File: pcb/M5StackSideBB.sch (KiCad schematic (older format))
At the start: 4 parts, among them J1 Conn_01x11, J2 Conn_01x11, J3 Conn_02x15_Odd_Even, J4 Conn_02x15_Odd_Even

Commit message: Assign footprint of pin socket without silk
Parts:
- J1, J2: footprint Connector_PinSocket_2.54mm:PinSocket_1x11_P2.54mm_Vertical -> footprints:PinSocket_1x11_P2.54mm_Vertical_without_silk
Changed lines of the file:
@@
 F 0 "J1" H 5150 3600 50  0000 L CNN
 F 1 "Conn_01x11" H 5000 3500 50  0000 L CNN
-F 2 "Connector_PinSocket_2.54mm:PinSocket_1x11_P2.54mm_Vertical" H 5150 2850 50  0001 C CNN
+F 2 "footprints:PinSocket_1x11_P2.54mm_Vertical_without_silk" H 5150 2850 50  0001 C CNN
 F 3 "~" H 5150 2850 50  0001 C CNN
 	1    5150 2850
@@
 F 0 "J2" H 6200 3600 50  0000 L CNN
 F 1 "Conn_01x11" H 6050 3500 50  0000 L CNN
-F 2 "Connector_PinSocket_2.54mm:PinSocket_1x11_P2.54mm_Vertical" H 6200 2850 50  0001 C CNN
+F 2 "footprints:PinSocket_1x11_P2.54mm_Vertical_without_silk" H 6200 2850 50  0001 C CNN
 F 3 "~" H 6200 2850 50  0001 C CNN
 	1    6200 2850
@@
 G34
 $Comp
-L power:+5V #PWR?
+L power:+5V #PWR0101
 U 1 1 5B50EF03
 P 7650 3600
-F 0 "#PWR?" H 7650 3450 50  0001 C CNN
+F 0 "#PWR0101" H 7650 3450 50  0001 C CNN
 F 1 "+5V" H 7665 3773 50  0000 C CNN
 F 2 "" H 7650 3600 50  0001 C CNN
@@
 	7900 3600 7650 3600
 $Comp
-L power:+BATT #PWR?
+L power:+BATT #PWR0102
 U 1 1 5B50EF0A
 P 7550 3700
-F 0 "#PWR?" H 7550 3550 50  0001 C CNN
+F 0 "#PWR0102" H 7550 3550 50  0001 C CNN
 F 1 "+BATT" H 7565 3873 50  0000 C CNN
 F 2 "" H 7550 3700 50  0001 C CNN
@@
 	8450 3600 8450 3500
 $Comp
-L power:GND #PWR?
+L power:GND #PWR0107
 U 1 1 5B50EF23
 P 8850 2500
-F 0 "#PWR?" H 8850 2250 50  0001 C CNN
+F 0 "#PWR0107" H 8850 2250 50  0001 C CNN
 F 1 "GND" H 8855 2327 50  0000 C CNN
 F 2 "" H 8850 2500 50  0001 C CNN
@@
 	8550 2400 8550 2500
 $Comp
-L power:+3.3V #PWR?
+L power:+3.3V #PWR0108
 U 1 1 5B50EF31
 P 7500 2800
-F 0 "#PWR?" H 7500 2650 50  0001 C CNN
+F 0 "#PWR0108" H 7500 2650 50  0001 C CNN
 F 1 "+3.3V" H 7515 2973 50  0000 C CNN
 F 2 "" H 7500 2800 50  0001 C CNN

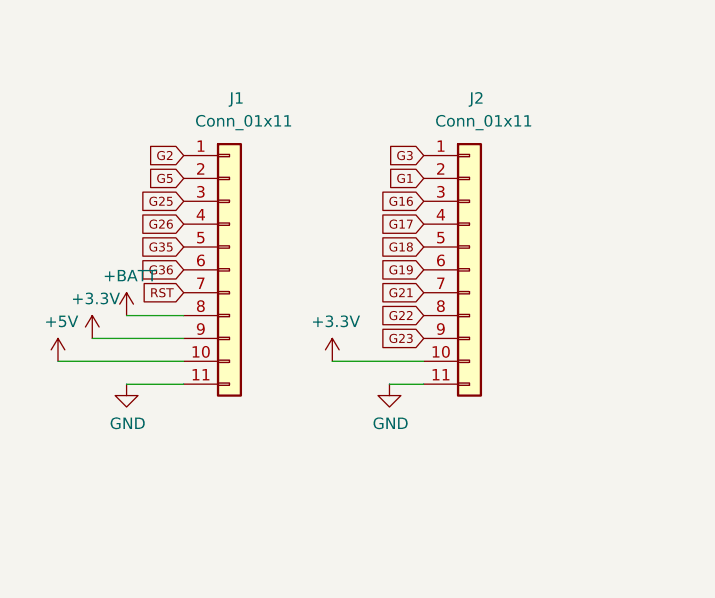
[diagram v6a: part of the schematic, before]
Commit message: Use 14 pins headers
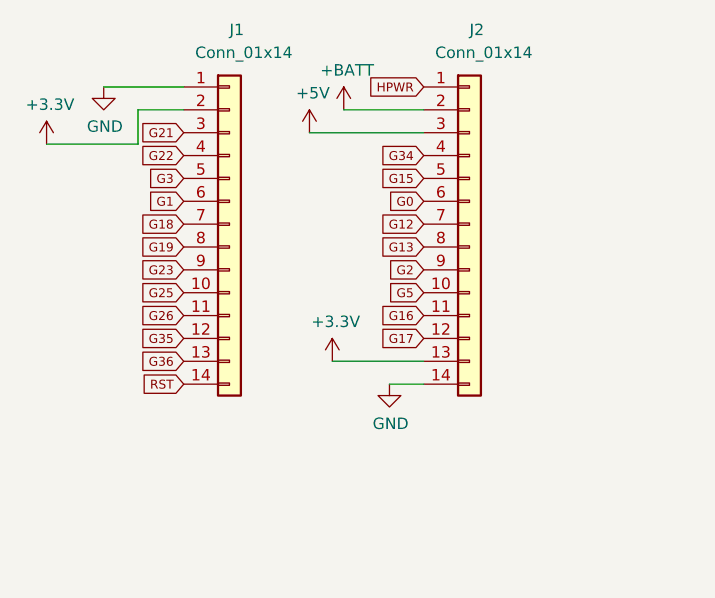
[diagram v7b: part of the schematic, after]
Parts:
- removed J1, J2: Conn_01x11, footprints:PinSocket_1x11_P2.54mm_Vertical_without_silk, symbol Connector_Generic:Conn_01x11
- added J1, J2: Conn_01x14, footprints:PinSocket_1x14_P2.54mm_Vertical_without_silk, symbol Connector_Generic:Conn_01x14
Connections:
- net +3V3: now also J1.2 (Pin_2), J2.13 (Pin_13)
- net +5V: now also J2.3 (Pin_3)
- net +BATT: now also J2.2 (Pin_2)
- net G0: now also J2.6 (Pin_6)
- net G1: now also J1.6 (Pin_6)
- net G12: now also J2.7 (Pin_7)
- net G13: now also J2.8 (Pin_8)
- net G15: now also J2.5 (Pin_5)
- net G16: now also J2.11 (Pin_11)
- net G17: now also J2.12 (Pin_12)
- net G18: now also J1.7 (Pin_7)
- net G19: now also J1.8 (Pin_8)
- net G2: now also J2.9 (Pin_9)
- net G21: now also J1.3 (Pin_3)
- net G22: now also J1.4 (Pin_4)
- net G23: now also J1.9 (Pin_9)
- net G25: now also J1.10 (Pin_10)
- net G26: now also J1.11 (Pin_11)
- net G3: now also J1.5 (Pin_5)
- net G34: now also J2.4 (Pin_4)
- net G35: now also J1.12 (Pin_12)
- net G36: now also J1.13 (Pin_13)
- net G5: now also J2.10 (Pin_10)
- net GND: now also J1.1 (Pin_1), J2.14 (Pin_14)
- net HPWR: now also J2.1 (Pin_1)
- net RST: now also J1.14 (Pin_14)
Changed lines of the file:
@@
 	1    0    0    -1
 $EndComp
+Text GLabel 6000 2850 0    39   Input ~ 0
+G2
+Text GLabel 4950 2250 0    39   Input ~ 0
+G21
+Text GLabel 6000 3050 0    39   Input ~ 0
+G16
+Text GLabel 4950 2450 0    39   Input ~ 0
+G3
+Text GLabel 4950 2650 0    39   Input ~ 0
+G18
+Text GLabel 4950 2750 0    39   Input ~ 0
+G19
+Text GLabel 4950 2850 0    39   Input ~ 0
+G23
+Text GLabel 4950 3150 0    39   Input ~ 0
+G35
+Text GLabel 4950 3250 0    39   Input ~ 0
+G36
+Text GLabel 4950 3350 0    39   Input ~ 0
+RST
+Text GLabel 4950 2950 0    39   Input ~ 0
+G25
+Text GLabel 4950 3050 0    39   Input ~ 0
+G26
+Text GLabel 4950 2550 0    39   Input ~ 0
+G1
+Text GLabel 6000 3150 0    39   Input ~ 0
+G17
 Text GLabel 4950 2350 0    39   Input ~ 0
-G2
+G22
 Text GLabel 6000 2950 0    39   Input ~ 0
-G21
-Text GLabel 6000 2550 0    39   Input ~ 0
-G16
-Text GLabel 6000 2350 0    39   Input ~ 0
-G3
-Text GLabel 6000 2750 0    39   Input ~ 0
-G18
-Text GLabel 6000 2850 0    39   Input ~ 0
-G19
-Text GLabel 6000 3150 0    39   Input ~ 0
-G23
-Text GLabel 4950 2750 0    39   Input ~ 0
-G35
-Text GLabel 4950 2850 0    39   Input ~ 0
-G36
-Text GLabel 4950 2950 0    39   Input ~ 0
-RST
-Text GLabel 4950 2550 0    39   Input ~ 0
-G25
-Text GLabel 4950 2650 0    39   Input ~ 0
-G26
-Text GLabel 6000 2450 0    39   Input ~ 0
-G1
-Text GLabel 6000 2650 0    39   Input ~ 0
-G17
-Text GLabel 6000 3050 0    39   Input ~ 0
-G22
-Text GLabel 4950 2450 0    39   Input ~ 0
 G5
 $Comp
 L power:+5V #PWR0103
 U 1 1 5B24B644
-P 4400 3250
-F 0 "#PWR0103" H 4400 3100 50  0001 C CNN
-F 1 "+5V" H 4415 3423 50  0000 C CNN
-F 2 "" H 4400 3250 50  0001 C CNN
-F 3 "" H 4400 3250 50  0001 C CNN
-	1    4400 3250
+P 5500 2250
+F 0 "#PWR0103" H 5500 2100 50  0001 C CNN
+F 1 "+5V" H 5515 2423 50  0000 C CNN
+F 2 "" H 5500 2250 50  0001 C CNN
+F 3 "" H 5500 2250 50  0001 C CNN
+	1    5500 2250
 	1    0    0    -1
 $EndComp
@@
 L power:+BATT #PWR0104
 U 1 1 5B24B943
-P 4700 3050
-F 0 "#PWR0104" H 4700 2900 50  0001 C CNN
-F 1 "+BATT" H 4715 3223 50  0000 C CNN
-F 2 "" H 4700 3050 50  0001 C CNN
-F 3 "" H 4700 3050 50  0001 C CNN
-	1    4700 3050
+P 5650 2150
+F 0 "#PWR0104" H 5650 2000 50  0001 C CNN
+F 1 "+BATT" H 5665 2323 50  0000 C CNN
+F 2 "" H 5650 2150 50  0001 C CNN
+F 3 "" H 5650 2150 50  0001 C CNN
+	1    5650 2150
 	1    0    0    -1
 $EndComp
@@
 L power:+3.3V #PWR0110
 U 1 1 5B27AF84
-P 4550 3150
-F 0 "#PWR0110" H 4550 3000 50  0001 C CNN
-F 1 "+3.3V" H 4565 3323 50  0000 C CNN
-F 2 "" H 4550 3150 50  0001 C CNN
-F 3 "" H 4550 3150 50  0001 C CNN
-	1    4550 3150
+P 4350 2300
+F 0 "#PWR0110" H 4350 2150 50  0001 C CNN
+F 1 "+3.3V" H 4365 2473 50  0000 C CNN
+F 2 "" H 4350 2300 50  0001 C CNN
+F 3 "" H 4350 2300 50  0001 C CNN
+	1    4350 2300
 	1    0    0    -1
 $EndComp
@@
 L power:GND #PWR0111
 U 1 1 5B27AFCA
-P 4700 3350
-F 0 "#PWR0111" H 4700 3100 50  0001 C CNN
-F 1 "GND" H 4705 3177 50  0000 C CNN
-F 2 "" H 4700 3350 50  0001 C CNN
-F 3 "" H 4700 3350 50  0001 C CNN
-	1    4700 3350
+P 4600 2050
+F 0 "#PWR0111" H 4600 1800 50  0001 C CNN
+F 1 "GND" H 4605 1877 50  0000 C CNN
+F 2 "" H 4600 2050 50  0001 C CNN
+F 3 "" H 4600 2050 50  0001 C CNN
+	1    4600 2050
 	1    0    0    -1
 $EndComp
@@
 Wire Wire Line
 	7900 4900 7500 4900
-Wire Wire Line
-	4950 3050 4700 3050
-Wire Wire Line
-	4950 3150 4550 3150
-Wire Wire Line
-	4950 3250 4400 3250
-Wire Wire Line
-	4950 3350 4700 3350
 $Comp
 L power:+3.3V #PWR0115
@@
 Wire Wire Line
 	6000 3250 5600 3250
-$Comp
-L Connector_Generic:Conn_01x11 J1
-U 1 1 5B50BA11
-P 5150 2850
-F 0 "J1" H 5150 3600 50  0000 L CNN
-F 1 "Conn_01x11" H 5000 3500 50  0000 L CNN
-F 2 "footprints:PinSocket_1x11_P2.54mm_Vertical_without_silk" H 5150 2850 50  0001 C CNN
-F 3 "~" H 5150 2850 50  0001 C CNN
-	1    5150 2850
-	1    0    0    -1
-$EndComp
-$Comp
-L Connector_Generic:Conn_01x11 J2
-U 1 1 5B50C22A
-P 6200 2850
-F 0 "J2" H 6200 3600 50  0000 L CNN
-F 1 "Conn_01x11" H 6050 3500 50  0000 L CNN
-F 2 "footprints:PinSocket_1x11_P2.54mm_Vertical_without_silk" H 6200 2850 50  0001 C CNN
-F 3 "~" H 6200 2850 50  0001 C CNN
-	1    6200 2850
-	1    0    0    -1
-$EndComp
 Wire Wire Line
 	6000 3350 5850 3350
@@
 Wire Wire Line
 	7900 2800 7500 2800
+Text GLabel 6000 2750 0    39   Input ~ 0
+G13
+Text GLabel 6000 2550 0    39   Input ~ 0
+G0
+Text GLabel 6000 2350 0    39   Input ~ 0
+G34
+Text GLabel 6000 2650 0    39   Input ~ 0
+G12
+Text GLabel 6000 2450 0    39   Input ~ 0
+G15
+Text GLabel 6000 2050 0    39   Input ~ 0
+HPWR
+$Comp
+L Connector_Generic:Conn_01x14 J1
+U 1 1 5C1CDEAB
+P 5150 2650
+F 0 "J1" H 5150 3500 50  0000 L CNN
+F 1 "Conn_01x14" H 5000 3400 50  0000 L CNN
+F 2 "footprints:PinSocket_1x14_P2.54mm_Vertical_without_silk" H 5150 2650 50  0001 C CNN
+F 3 "~" H 5150 2650 50  0001 C CNN
+	1    5150 2650
+	1    0    0    -1
+$EndComp
+$Comp
+L Connector_Generic:Conn_01x14 J2
+U 1 1 5C1CDF6E
+P 6200 2650
+F 0 "J2" H 6200 3500 50  0000 L CNN
+F 1 "Conn_01x14" H 6050 3400 50  0000 L CNN
+F 2 "footprints:PinSocket_1x14_P2.54mm_Vertical_without_silk" H 6200 2650 50  0001 C CNN
+F 3 "~" H 6200 2650 50  0001 C CNN
+	1    6200 2650
+	1    0    0    -1
+$EndComp
+Wire Wire Line
+	4950 2050 4600 2050
+Wire Wire Line
+	4950 2150 4750 2150
+Wire Wire Line
+	4750 2150 4750 2300
+Wire Wire Line
+	4750 2300 4350 2300
+Wire Wire Line
+	5500 2250 6000 2250
+Wire Wire Line
+	6000 2150 5650 2150
 $EndSCHEMATC

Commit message: Remove redundant top pad
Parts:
- J3: footprint footprints:PinHeader_2x15_P2.54mm_Vertical_SMD_for_M5Stack_top -> footprints:PinHeader_2x15_P2.54mm_Vertical_SMD_for_M5Stack_top_only_round_pads
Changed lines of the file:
@@
 F 0 "J3" H 8150 3917 50  0000 C CNN
 F 1 "Conn_02x15_Odd_Even" H 8150 3826 50  0000 C CNN
-F 2 "footprints:PinHeader_2x15_P2.54mm_Vertical_SMD_for_M5Stack_top" H 8100 3000 50  0001 C CNN
+F 2 "footprints:PinHeader_2x15_P2.54mm_Vertical_SMD_for_M5Stack_top_only_round_pads" H 8100 3000 50  0001 C CNN
 F 3 "~" H 8100 3000 50  0001 C CNN
 	1    8100 3000
